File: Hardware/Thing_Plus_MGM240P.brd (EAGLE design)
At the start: 22.9 x 58.4 mm, 140 parts, among them J1 THING_PLUS_LOGICAL, J2 USB Female Type C Connector, J3 QWIIC_RIGHT_ANGLE, J5 MICRO-SDFRICTION, Q1 20V/4.2A/52mΩ/1.4W, Q2 20V/4.2A/52mΩ/1.4W, U1 MGM240P, U2 XC6222B331MR-G, U4 MCP73831, U5 MAX17048, U6 MK22FN128VLH10

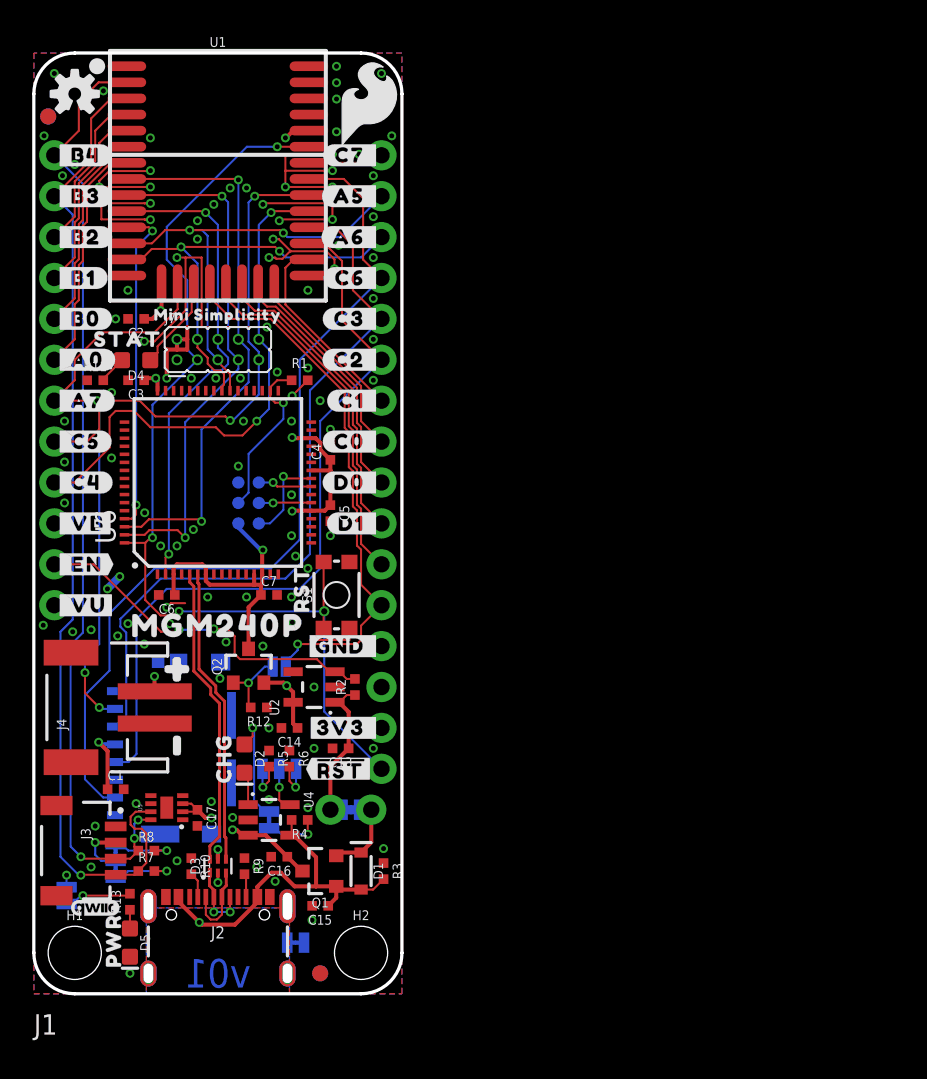
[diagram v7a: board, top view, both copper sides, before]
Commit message: Design review and checklist updates
Swap J-Link test points for new part
Change size of STAT silk and add pin number
Adjust fuel gauge cap position
Adjust board name silk positions
Add ordering instructions (4 layer board)
Improve GND continuity
Add layer numbers in copper
Move LED jumper out of standoff keepout
Update charge current silk labels to read "0.5A" instead of 500
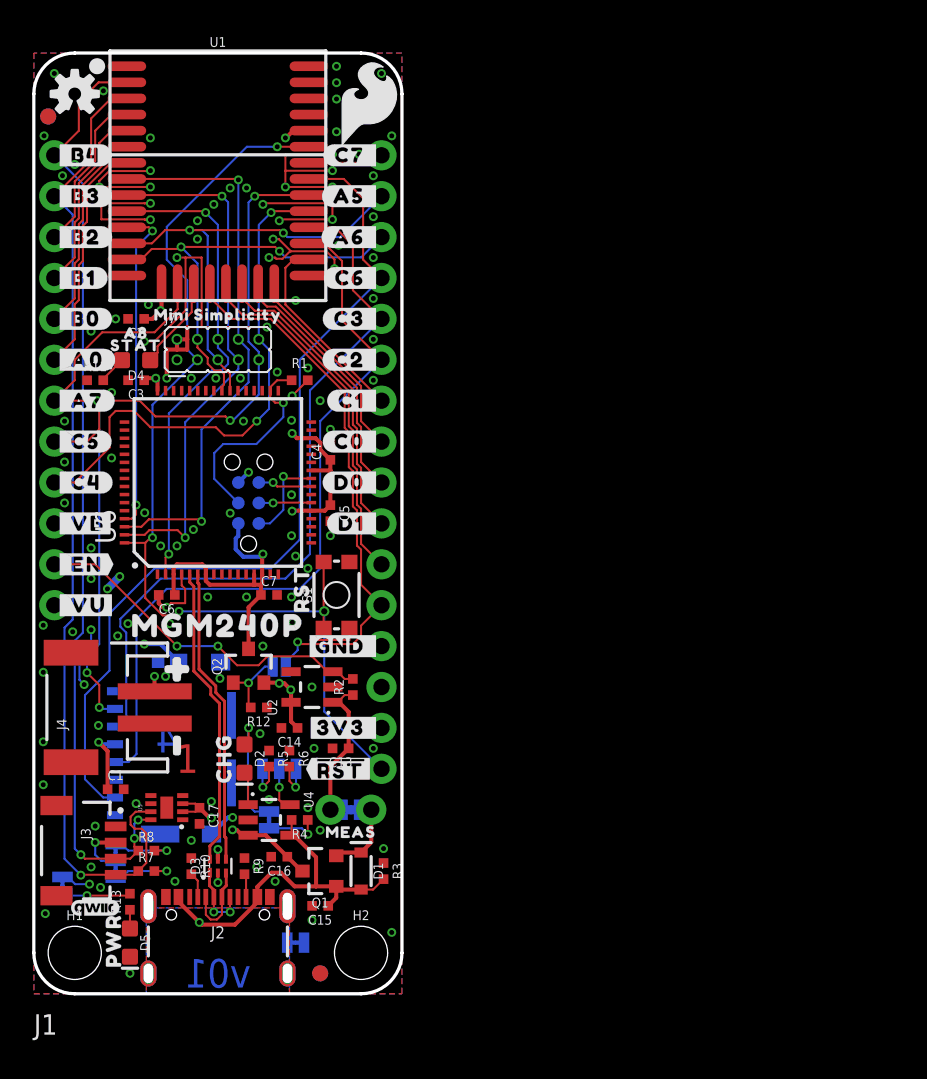
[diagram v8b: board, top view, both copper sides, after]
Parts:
- removed TP1, TP2, TP3, TP4, TP5, TP6: TEST-POINT3, SparkFun-Connectors:PAD.03X.03
- added J6: CONN_03X2, J_LINK_6_PIN:2X3_J_LINK_6_PIN
- added U$72: (no value), output:A80
- added U$75: (no value), SparkFun-Aesthetics:ORDERING_INSTRUCTIONS
- added U$76: (no value), SparkFun-Aesthetics:FOUR_LAYER_WARNING
- U$63: device output:#500#0 -> output:#0#5A#0
- U$64: device output:#100#0 -> output:#0#1A#0
- U$66: device output:_1 -> output:MEAS81
- moved U$66 20.0 mm to (19.7, 10.0), flipped to the top
- moved PWR 0.68 mm to (1.78, 6.73)
- moved U$19 0.68 mm to (1.78, 7.62)
- moved U$58 0.64 mm to (11.4, 34.4)
- moved U$68 0.64 mm to (6.35, 40.3)
- moved C17 0.18 mm to (10.3, 11.0)
- moved U$69 0.13 mm to (11.4, 37.0)
- moved U2 0.13 mm to (17.3, 19.1)
- moved R2 0.13 mm to (19.8, 19.1)
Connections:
- net !DBG_RESET!: now also J6.3; no longer TP3.1
- net DBG_SWCLK: now also J6.4; no longer TP4.1
- net DBG_SWDIO: now also J6.2; no longer TP2.1
- net DBG_SWO: now also J6.6; no longer TP6.1
- net GND: now also J6.5; no longer TP5.1
- net VDD: now also J6.1; no longer TP1.1
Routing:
- net GND: track 69.9 -> 82.0 mm, vias 107 -> 121
- net !DBG_RESET!: track 10.5 -> 12.9 mm
- net 3.3V: track 16.8 -> 18.0 mm, vias 7 -> 8
- net VDD: track 46.3 -> 47.4 mm
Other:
- board text added: "1"
- board text added: "2"
- board text added: "3"
- board text added: "4"
